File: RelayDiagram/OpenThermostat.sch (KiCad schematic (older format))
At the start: 87 parts, among them J1 Conn_01x08_Female, J2 Conn_01x15_Female, J3 Conn_01x15_Female, J4 Conn_01x09_Female, Q1 Q_NMOS_DGS, Q10 Q_NMOS_DGS, Q11 Q_NMOS_DGS, Q12 Q_NMOS_DGS, Q2 Q_NMOS_DGS, Q3 Q_NMOS_DGS, Q4 Q_NMOS_DGS, Q5 Q_NMOS_DGS, Q6 Q_NMOS_DGS, Q7 Q_NMOS_DGS, Q8 Q_NMOS_DGS, Q9 Q_NMOS_DGS, SW2 SW_Push, SW3 SW_Push, SW4 SW_Push, SW5 SW_Push, SW6 SW_Push, U1 PCF8574, U2 LCD, U3 DHT11, U4 EE2-3TNU-L_DPDT_Relay, U5 EE2-3TNU-L_DPDT_Relay, U6 EE2-3TNU-L_DPDT_Relay, U7 EE2-3TNU-L_DPDT_Relay, U8 EE2-3TNU-L_DPDT_Relay, U9 EE2-3TNU-L_DPDT_Relay

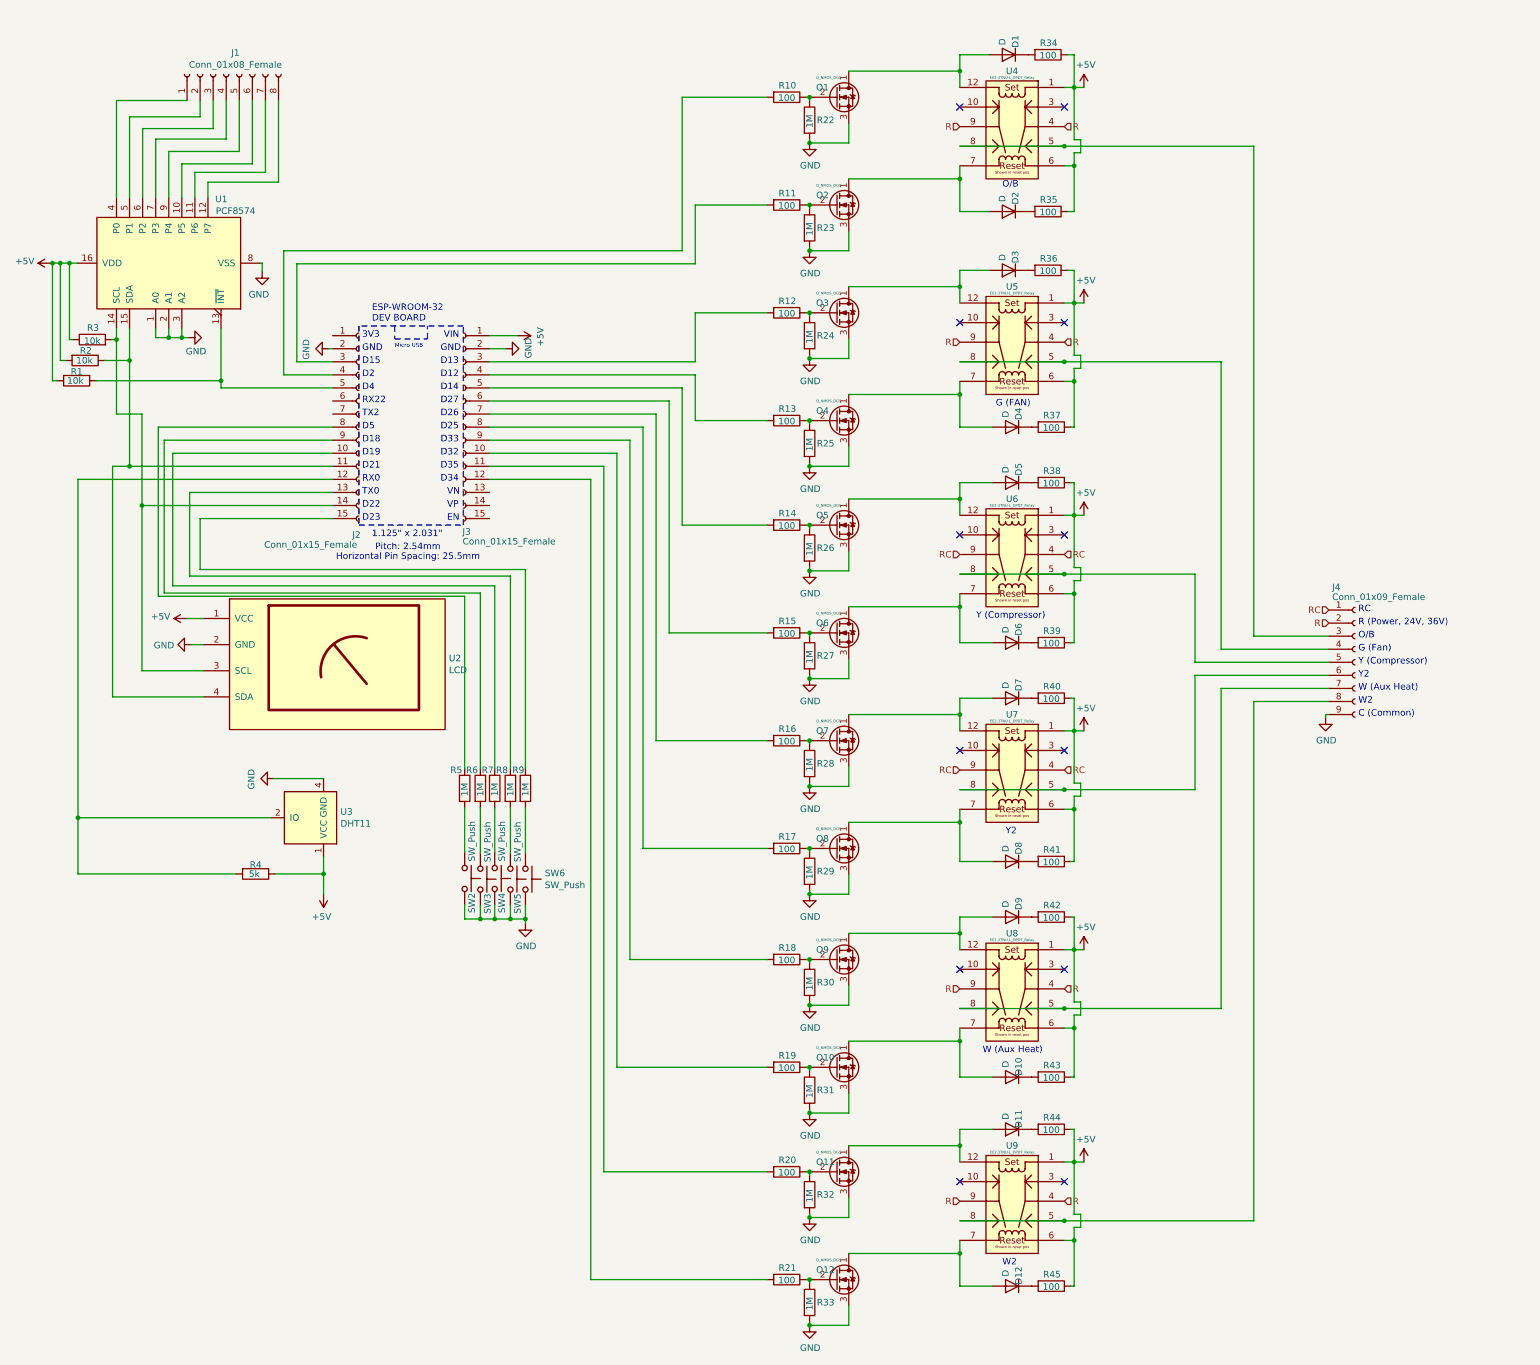
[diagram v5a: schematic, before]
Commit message: Added Power Components to schematic, Added Footprints
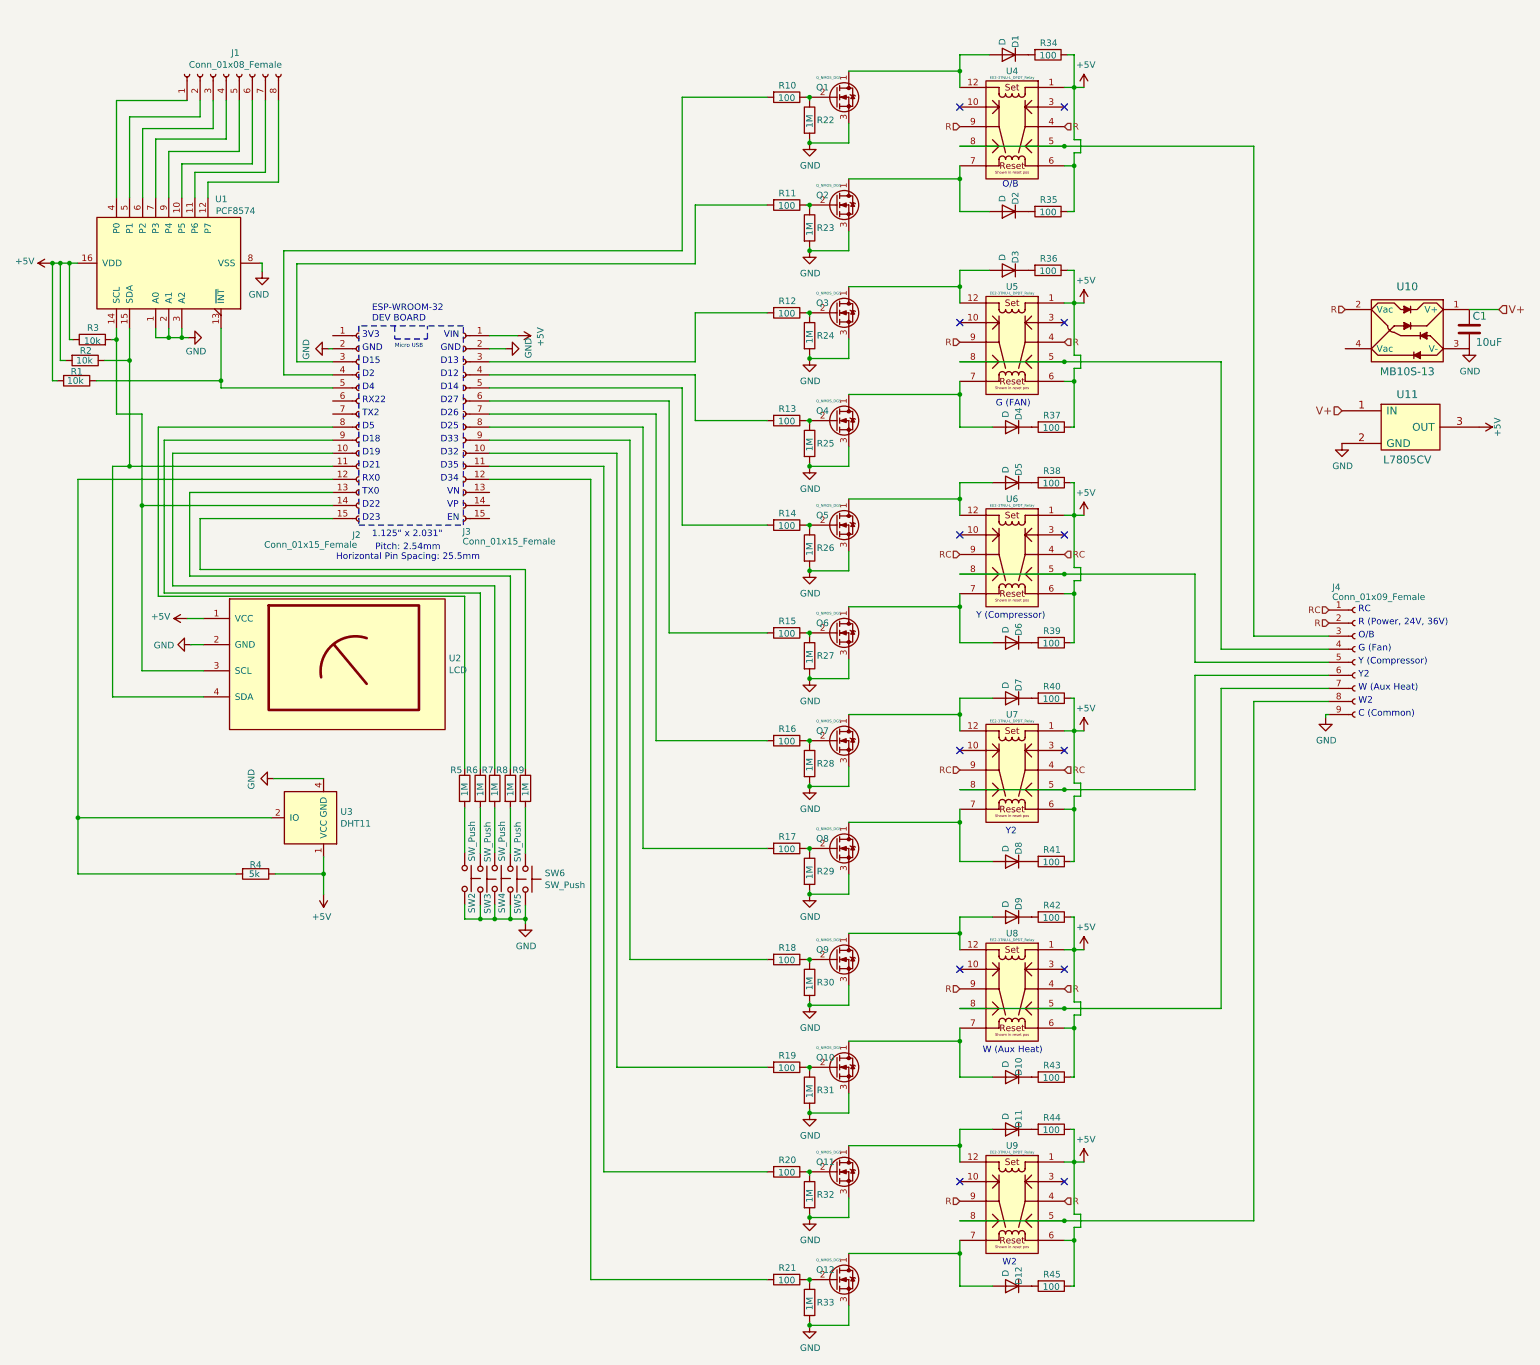
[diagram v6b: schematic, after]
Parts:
- added C1: 10uF, solarcar-device:Capacitor_0805, symbol Capacitor_Unpolarized
- added U10: MB10S-13, Open_Thermostat:MB10F-13, symbol MB10S-13
- added U11: L7805CV, Open_Thermostat:L7805CV, symbol L7805CV
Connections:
- net +5V: now also U11.3 (OUT)
- net GND: now also C1.2, U10.3 (V-), U11.2 (GND)
- net R: now also U10.2 (Vac)
- new net V+: C1.1, U10.1 (V+), U11.1 (IN)

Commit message: Fixed broken schematic
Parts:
- C1: symbol Capacitor_Unpolarized -> solarcar-device:Capacitor_Unpolarized
- U10: symbol MB10S-13 -> OpenThermostat-rescue:MB10S-13
- U11: symbol L7805CV -> OpenThermostat-rescue:L7805CV

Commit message: Relay updates
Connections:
- net at U4.5, U4.8: now also J4.6 (Pin_6); no longer J4.3 (Pin_3)
- net at U5.5, U5.8: now also J4.5 (Pin_5); no longer J4.4 (Pin_4)
- net at U6.5, U6.8: now also J4.8 (Pin_8); no longer J4.5 (Pin_5)
- net at U7.5, U7.8: now also J4.7 (Pin_7); no longer J4.6 (Pin_6)
- net at U8.5, U8.8: now also J4.4 (Pin_4); no longer J4.7 (Pin_7)
- net at U9.5, U9.8: now also J4.3 (Pin_3); no longer J4.8 (Pin_8)
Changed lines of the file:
@@
 Text Notes 7875 9850 0    50   ~ 0
 W2
-Text Notes 10600 5050 0    50   ~ 0
+Text Notes 10600 5350 0    50   ~ 0
 O/B
+Text Notes 10600 5250 0    50   ~ 0
+G (Fan)
+Text Notes 10600 5550 0    50   ~ 0
+Y (Compressor)
 Text Notes 10600 5150 0    50   ~ 0
-G (Fan)
-Text Notes 10600 5250 0    50   ~ 0
-Y (Compressor)
-Text Notes 10600 5450 0    50   ~ 0
 W (Aux Heat)
 Text Notes 10600 5650 0    50   ~ 0
@@
 Text Notes 10600 4850 0    50   ~ 0
 RC
-Text Notes 10600 5550 0    50   ~ 0
+Text Notes 10600 5050 0    50   ~ 0
 W2
-Text Notes 10600 5350 0    50   ~ 0
+Text Notes 10600 5450 0    50   ~ 0
 Y2
 $Comp
@@
 	7550 1275 8350 1275
 Wire Wire Line
-	9800 1275 9800 5025
-Wire Wire Line
-	9800 5025 10375 5025
-Wire Wire Line
 	7550 2925 8350 2925
 Wire Wire Line
-	9550 2925 9550 5125
-Wire Wire Line
-	9550 5125 10375 5125
-Wire Wire Line
 	7550 4550 8350 4550
 Wire Wire Line
-	9350 4550 9350 5225
-Wire Wire Line
-	9350 5225 10375 5225
-Wire Wire Line
-	9350 5325 10375 5325
-Wire Wire Line
 	7550 7875 8350 7875
 Wire Wire Line
-	9550 7875 9550 5425
-Wire Wire Line
-	9550 5425 10375 5425
-Wire Wire Line
 	7550 9500 8350 9500
-Wire Wire Line
-	9800 9500 9800 5525
-Wire Wire Line
-	9800 5525 10375 5525
 Wire Wire Line
 	2750 2925 2475 2925
@@
 	7550 6200 8350 6200
 Wire Wire Line
-	9350 6200 9350 5325
-Wire Wire Line
 	1290 5290 1760 5290
 Wire Wire Line
@@
 Wire Wire Line
 	1095 925  1635 925
-Connection ~ 8350 1275
-Connection ~ 8350 2925
-Connection ~ 8350 4550
 Connection ~ 8350 6200
 Connection ~ 8350 7875
@@
 	605  2170 665  2170
 Wire Wire Line
-	8350 1275 9800 1275
-Wire Wire Line
-	8350 2925 9550 2925
-Wire Wire Line
-	8350 4550 9350 4550
-Wire Wire Line
 	8350 6200 9350 6200
 Wire Wire Line
@@
 Wire Wire Line
 	10500 2825 10400 2825
+Wire Wire Line
+	9800 5025 10375 5025
+Wire Wire Line
+	9800 5025 9800 9500
+Wire Wire Line
+	9550 5125 9750 5125
+Wire Wire Line
+	9750 5125 9750 5175
+Wire Wire Line
+	9750 5175 9850 5175
+Wire Wire Line
+	9850 5175 9850 5125
+Wire Wire Line
+	9850 5125 10375 5125
+Wire Wire Line
+	9550 5125 9550 7875
+Wire Wire Line
+	10375 5225 9850 5225
+Wire Wire Line
+	9850 5225 9850 5275
+Wire Wire Line
+	9850 5275 9750 5275
+Wire Wire Line
+	9750 5275 9750 5225
+Wire Wire Line
+	9750 5225 9600 5225
+Wire Wire Line
+	9600 5225 9600 5275
+Wire Wire Line
+	9600 5275 9500 5275
+Wire Wire Line
+	9500 5275 9500 2925
+Wire Wire Line
+	9500 2925 8350 2925
+Connection ~ 8350 2925
+Wire Wire Line
+	10375 5325 9850 5325
+Wire Wire Line
+	9850 5325 9850 5375
+Wire Wire Line
+	9850 5375 9750 5375
+Wire Wire Line
+	9750 5375 9750 5325
+Wire Wire Line
+	9750 5325 9600 5325
+Wire Wire Line
+	9600 5325 9600 5375
+Wire Wire Line
+	9600 5375 9500 5375
+Wire Wire Line
+	9500 5375 9500 5325
+Wire Wire Line
+	9500 5325 9325 5325
+Wire Wire Line
+	9325 5325 9325 3000
+Wire Wire Line
+	9325 3000 9250 3000
+Wire Wire Line
+	9250 3000 9250 2850
+Wire Wire Line
+	9250 2850 9325 2850
+Wire Wire Line
+	9325 2850 9325 1275
+Wire Wire Line
+	9325 1275 8350 1275
+Connection ~ 8350 1275
+Wire Wire Line
+	9350 6200 9350 5425
+Wire Wire Line
+	9350 5425 9500 5425
+Wire Wire Line
+	9500 5425 9500 5475
+Wire Wire Line
+	9500 5475 9600 5475
+Wire Wire Line
+	9600 5475 9600 5425
+Wire Wire Line
+	9600 5425 9750 5425
+Wire Wire Line
+	9750 5425 9750 5475
+Wire Wire Line
+	9750 5475 9850 5475
+Wire Wire Line
+	9850 5475 9850 5425
+Wire Wire Line
+	9850 5425 10375 5425
+Wire Wire Line
+	9850 5525 9850 5575
+Wire Wire Line
+	9850 5575 9750 5575
+Wire Wire Line
+	9750 5575 9750 5525
+Wire Wire Line
+	9750 5525 9600 5525
+Wire Wire Line
+	9600 5525 9600 5575
+Wire Wire Line
+	9600 5575 9500 5575
+Wire Wire Line
+	9500 5575 9500 5525
+Wire Wire Line
+	9500 5525 9400 5525
+Wire Wire Line
+	9400 5525 9400 5575
+Wire Wire Line
+	9400 5575 9300 5575
+Wire Wire Line
+	9300 5575 9300 5525
+Wire Wire Line
+	9300 5525 9125 5525
+Wire Wire Line
+	9125 5525 9125 4550
+Wire Wire Line
+	9125 4550 8350 4550
+Connection ~ 8350 4550
+Wire Wire Line
+	9850 5525 10375 5525
 $EndSCHEMATC
